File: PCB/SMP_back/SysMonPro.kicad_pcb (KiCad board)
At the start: 2 copper layers, 100 x 97.5 mm, 20 parts, among them J1 V0+, J2 V1+, J3 V2+, J4 Conn_02x03_Counter_Clockwise, J5 V0-, J6 V1-, J7 V2-, J8 V3-, J9 V3+, P1 USB_C_Plug_USB2.0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

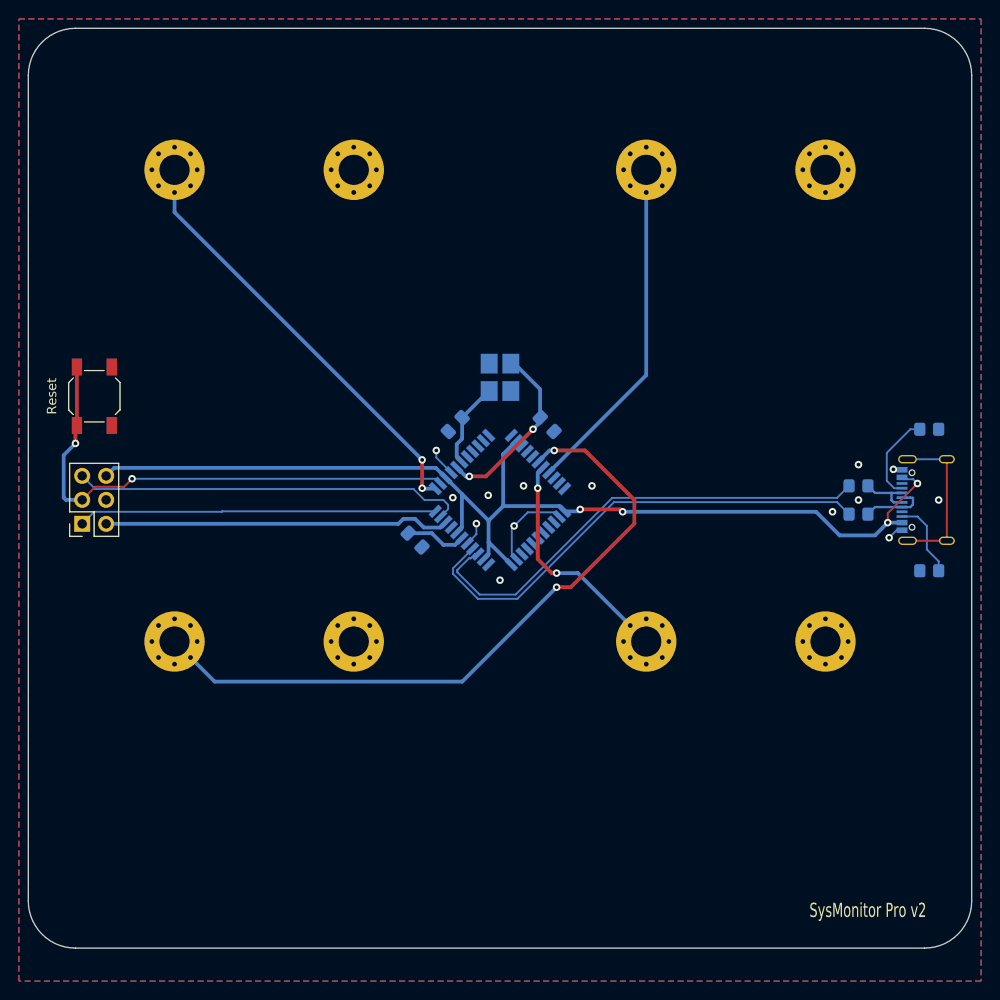
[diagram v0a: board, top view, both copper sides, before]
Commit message: enlarged hole
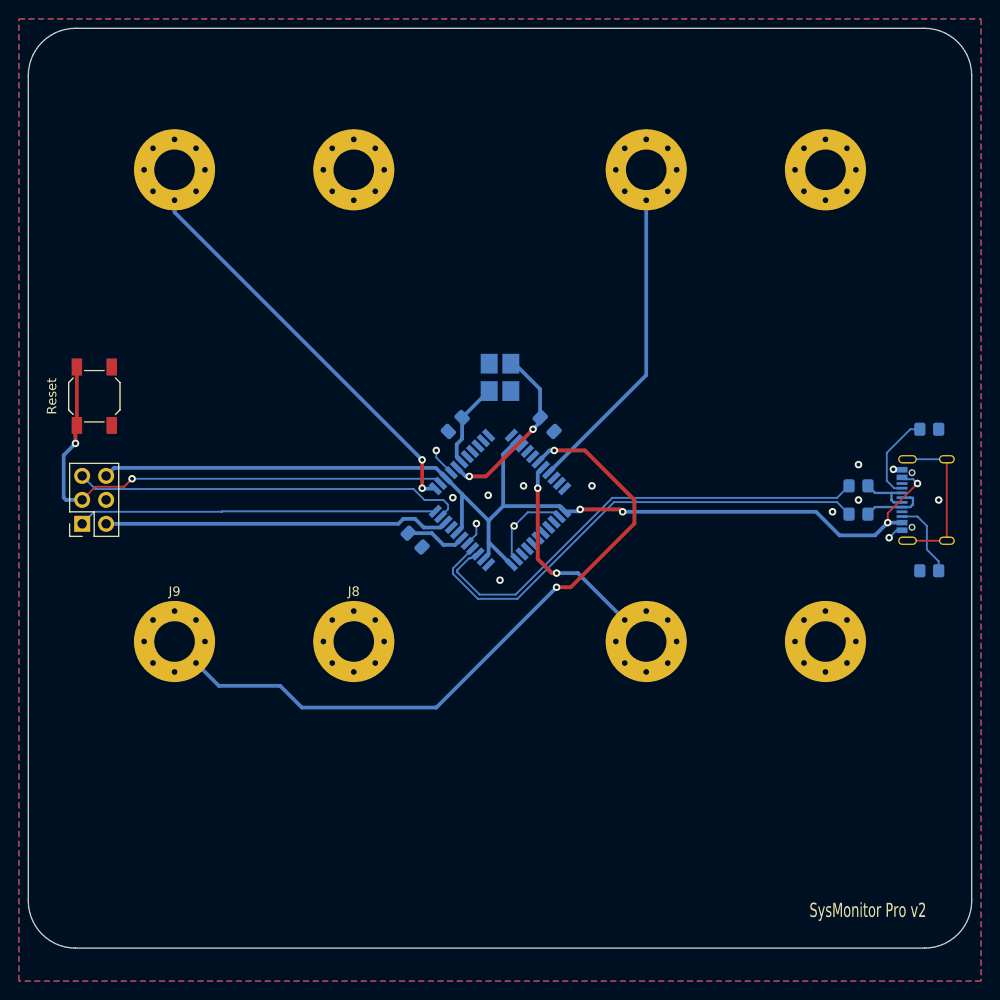
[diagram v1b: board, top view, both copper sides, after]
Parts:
- J1, J2, J3, J5, J6, J7, J8, J9: footprint MountingHole:MountingHole_3.2mm_M3_Pad_Via -> MountingHole:MountingHole_4.3mm_M4_Pad_Via
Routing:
- net Net-(J9-Pad1): track 72.8 -> 75.1 mm
